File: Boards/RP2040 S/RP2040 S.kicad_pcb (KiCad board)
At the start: 4 copper layers, 60 x 22 mm, 75 parts, among them J1 BM03B-SRSS-TBLFSN, J2 BM03B-SRSS-TBLFSN, J3 USB_C, J4 DX07S016JA1R1500, SW1 SW_Push, SW3 SW_Push, U1 ESD7L5.0DT5G, U1 ST1L05APU33R, U2 ST1L05APU33R, U2 W25Q128JVSIQ TR, U3 ESD7L5.0DT5G

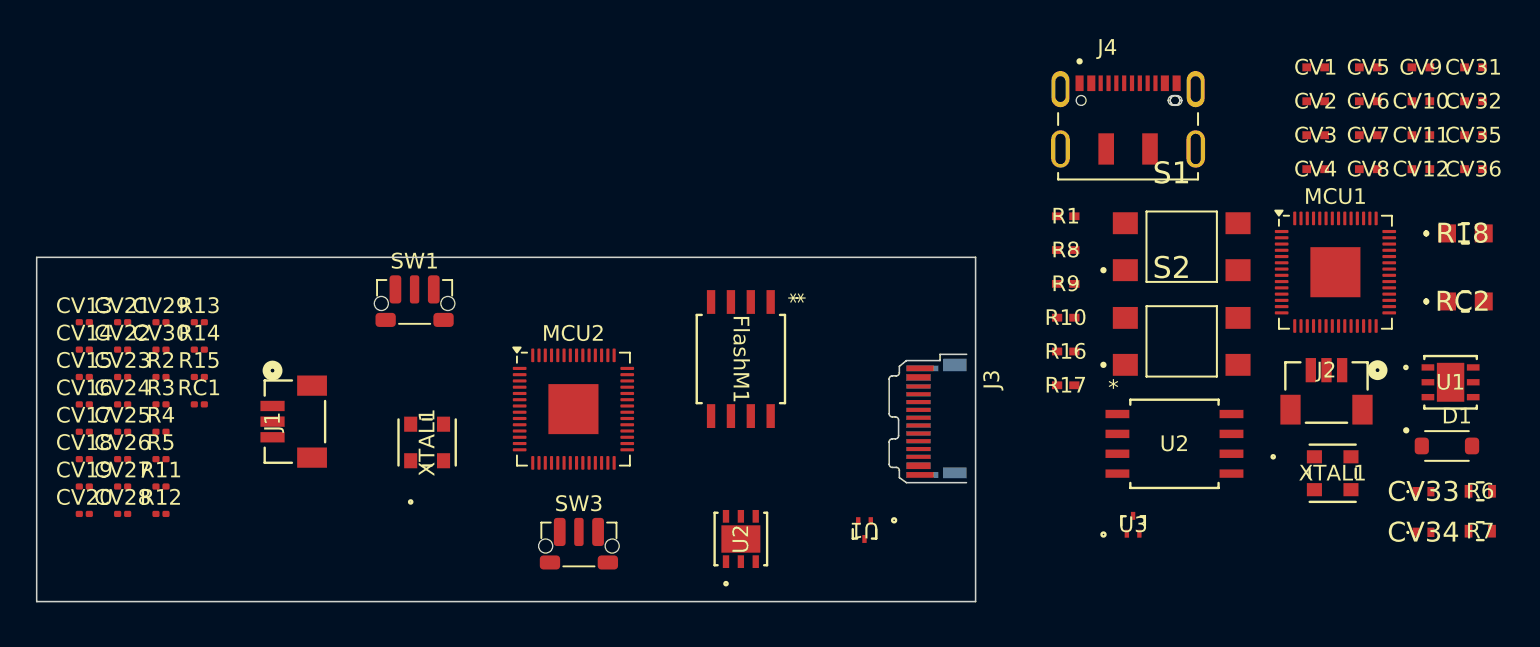
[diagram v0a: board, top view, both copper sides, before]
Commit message: Sockets Pico_Conn
Adição à Library e ao RP2040 S de Sockets iguais às placas de Pico.
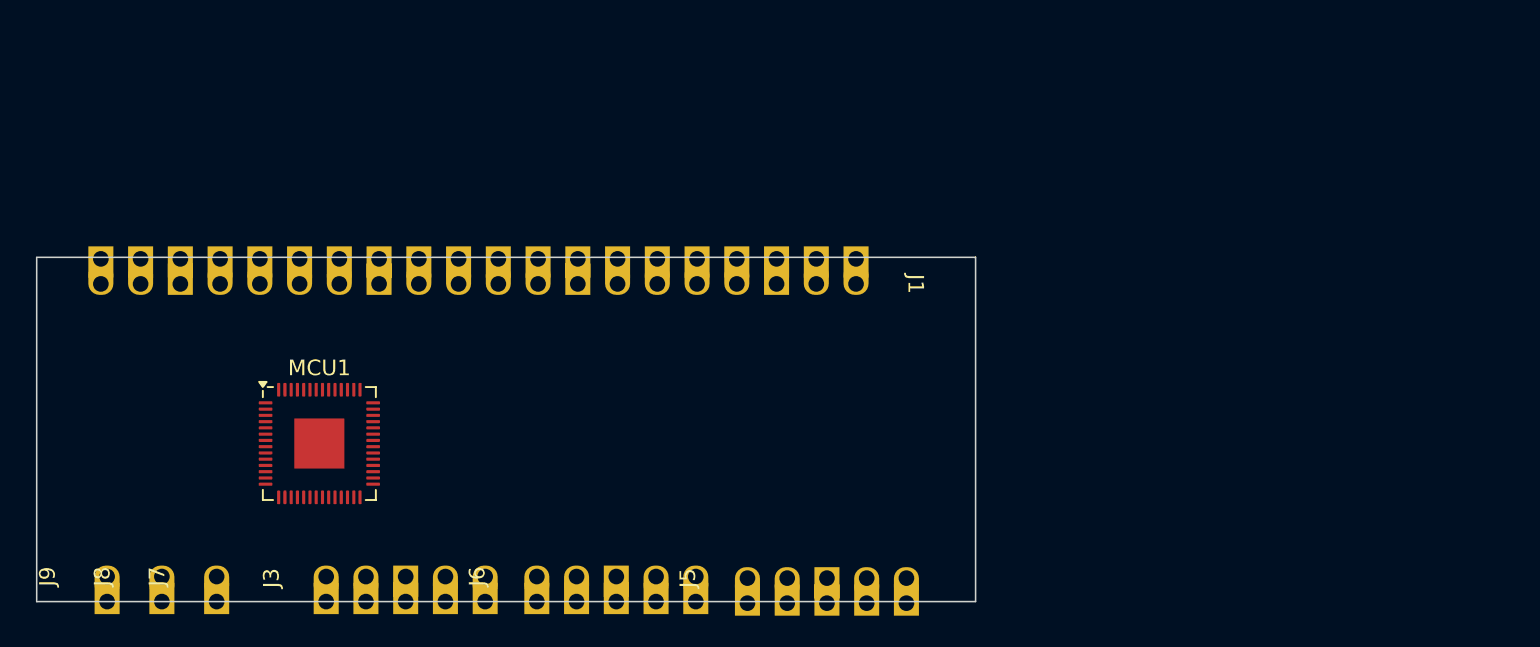
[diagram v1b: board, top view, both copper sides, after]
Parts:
- removed CV1, CV3, CV31, CV35, CV6: 1uF, Capacitor_0402:Capacitor_0402
- removed CV10, CV11, CV12, CV2, CV32, CV36, CV4, CV5, CV7, CV8, CV9: 100nF, Capacitor_0402:Capacitor_0402
- removed CV13, CV15, CV18, CV25, CV29: 1uF, Capacitor_SMD:C_0201_0603Metric
- removed CV14, CV16, CV17, CV19, CV20, CV21, CV22, CV23, CV24, CV26, CV30: 100nF, Capacitor_SMD:C_0201_0603Metric
- removed CV27, CV28: 4.7uF, Capacitor_SMD:C_0201_0603Metric
- removed CV33, CV34: 4.7uF, C_4uF7_0402:C_4uF7_0402
- removed D1: PMEG2010ER, PMEG2010ER:SODFL3517X110N
- removed FlashM1: W25Q128JVSIQ_TR, NOR Flash:SOIC_208MIL_WIN
- removed J2: BM03B-SRSS-TBLFSN, SWD_Con:CONN_BM03B-SRSS-TBLFSN_JST
- removed J4: DX07S016JA1R1500, USBC-DX07S016JA1:JAE_DX07S016JA1R1500
- removed MCU2: RP2040, Package_DFN_QFN:QFN-56-1EP_7x7mm_P0.4mm_EP3.2x3.2mm
- removed R1, R10, R17: 1k, RES_0402:RES_0402
- removed R11, R5: 100, Resistor_SMD:R_0201_0603Metric
- removed R12, R14, R2: 1k, Resistor_SMD:R_0201_0603Metric
- removed R13: 10k, Resistor_SMD:R_0201_0603Metric
- removed R15, RC1: 5k1, Resistor_SMD:R_0201_0603Metric
- removed R16: 10k, RES_0402:RES_0402
- removed R18, RC2: 5k1, R_0805_5K1:R_0805_5K1
- removed R3, R4: 27, Resistor_SMD:R_0201_0603Metric
- removed R6, R7: 27, RES_R0603_27:RES_R0603_27
- removed R8, R9: 100, RES_0402:RES_0402
- removed S1, S2: TL3305CF160QG, E-Switch_7mm:SW_TL3305CF160QG
- removed SW1, SW3: SW_Push, Button_Switch_SMD:SW_Push_1P1T-MP_NO_Horizontal_Alps_SKRTLAE010
- removed U1, U3: ESD7L5.0DT5G, ESD7L5-Diode:SOT-723_0P85X1P25_ONS
- removed U1, U2: ST1L05APU33R, LDO ST1L05A:DFN_5APU33R_STM
- removed U2: W25Q128JVSIQ TR, NOR Flash:SOIC_208MIL_WIN
- removed XTAL1 (x2): ASE-12.000MHZ-LC-T, AS12MHz:ASE-3.2X2.5_ABR
- added J5: Conn_01x05_Socket, Pico_Conn1x5:Pico_05pin, F.Cu at (157.4, 76.5)
- added J6: Conn_01x05_Socket, Pico_Conn1x5:Pico_05pin, F.Cu at (144.0, 76.4)
- added J7: Conn_01x01_Socket, Pico_Conn1x1:Pico_01pin, F.Cu at (123.5, 76.4)
- added J8: Conn_01x01_Socket, Pico_Conn1x1:Pico_01pin, F.Cu at (120.0, 76.4)
- added J9: Conn_01x01_Socket, Pico_Conn1x1:Pico_01pin, F.Cu at (116.5, 76.4)
- J1: value BM03B-SRSS-TBLFSN -> Conn_01x20_Socket; footprint SWD_Con:CONN_BM03B-SRSS-TBLFSN_JST -> Pico_Conn1x20:Pico_20pin
- J3: value USB_C -> Conn_01x05_Socket; footprint Connector_USB:USB_C_Plug_JAE_DX07P024AJ1 -> Pico_Conn1x5:Pico_05pin
- moved MCU1 65.8 mm to (130.1, 67.9)
- moved J3 40.2 mm to (130.5, 76.4), turned to 90 degrees
- moved J1 36.9 mm to (164.4, 57.7), turned to -90 degrees
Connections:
- net /RP2040 Standard/GP25/PWM4 B renamed Net-(MCU1-GPIO25)
- J1 pad 1: Net-(J1-Pad1) -> /RP2040 Standard/GP15/I2C1 SCL
- J1 pad 2: GND -> /RP2040 Standard/GP14/I2C1 SDA
- J1 pad 3: Net-(J1-Pad3) -> GND
- J1 pad 4: (no net) -> /RP2040 Standard/GP13/I2C0 SCL
- J1 pad 5: (no net) -> /RP2040 Standard/GP12/I2C0 SDA
